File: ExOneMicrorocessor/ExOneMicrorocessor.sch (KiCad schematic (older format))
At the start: 33 parts, among them IC1 STM32G041C8T6, IC2 FT230XS, IC3 TLV73333PQDBVRQ1, J1 UJ2-MBH-3-SMT, J2 Conn_01x02, J3 02x03 Header, J4 01x03, J5 01x08, J6 01x10, J7 01x12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

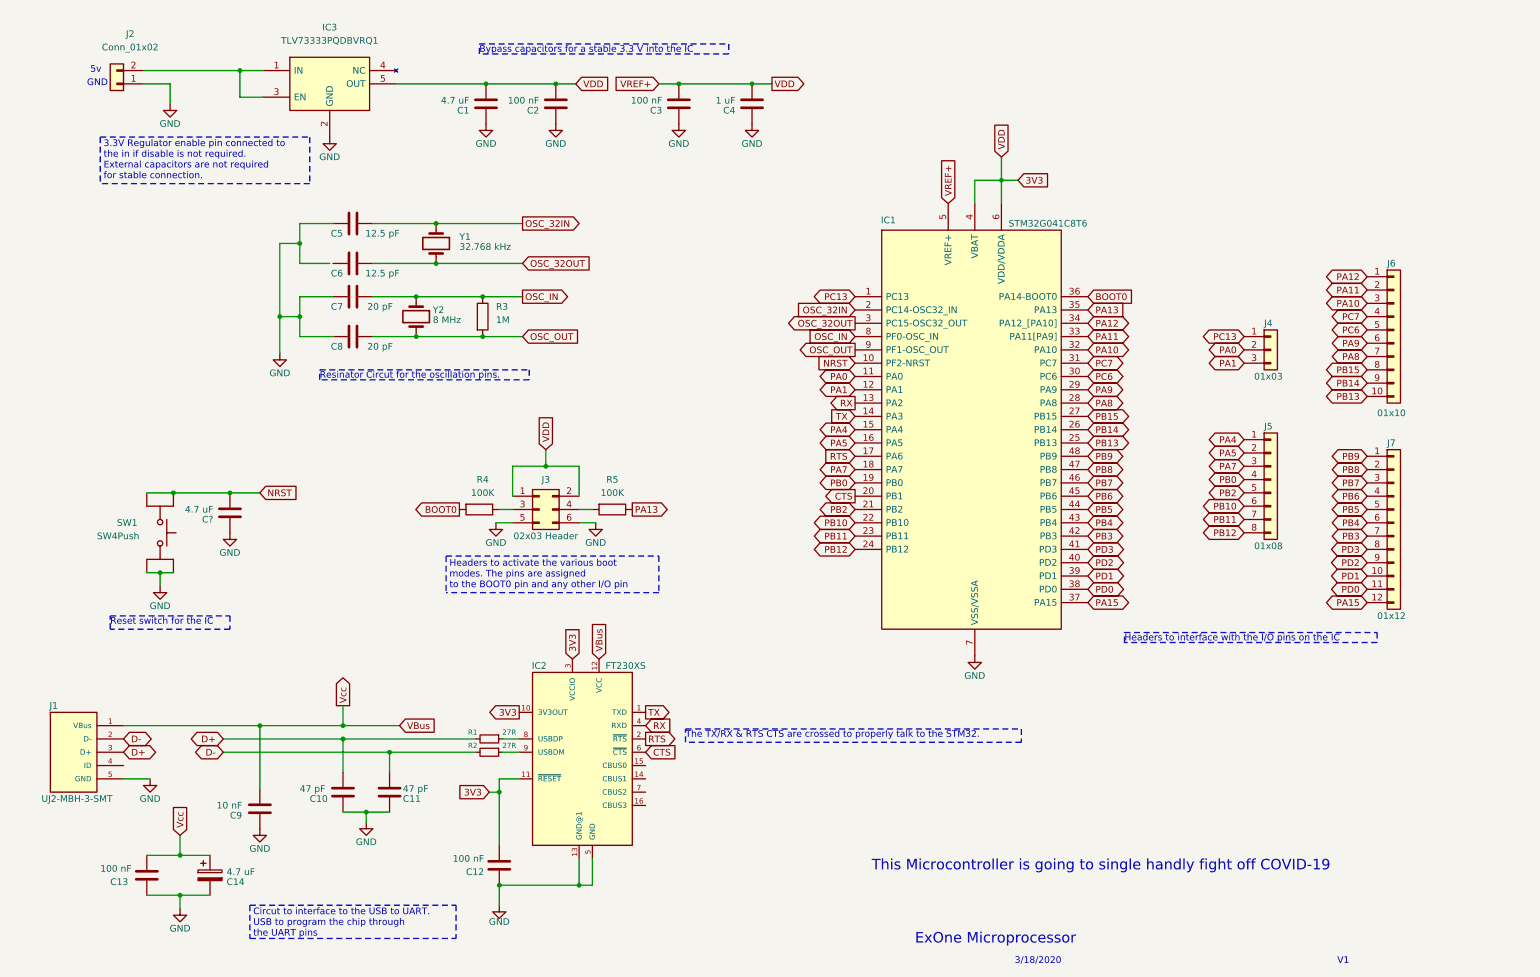
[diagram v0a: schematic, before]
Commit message: Updated Schematic
Updated net names

Added various notes explaning the design further

Changed the LDO IC
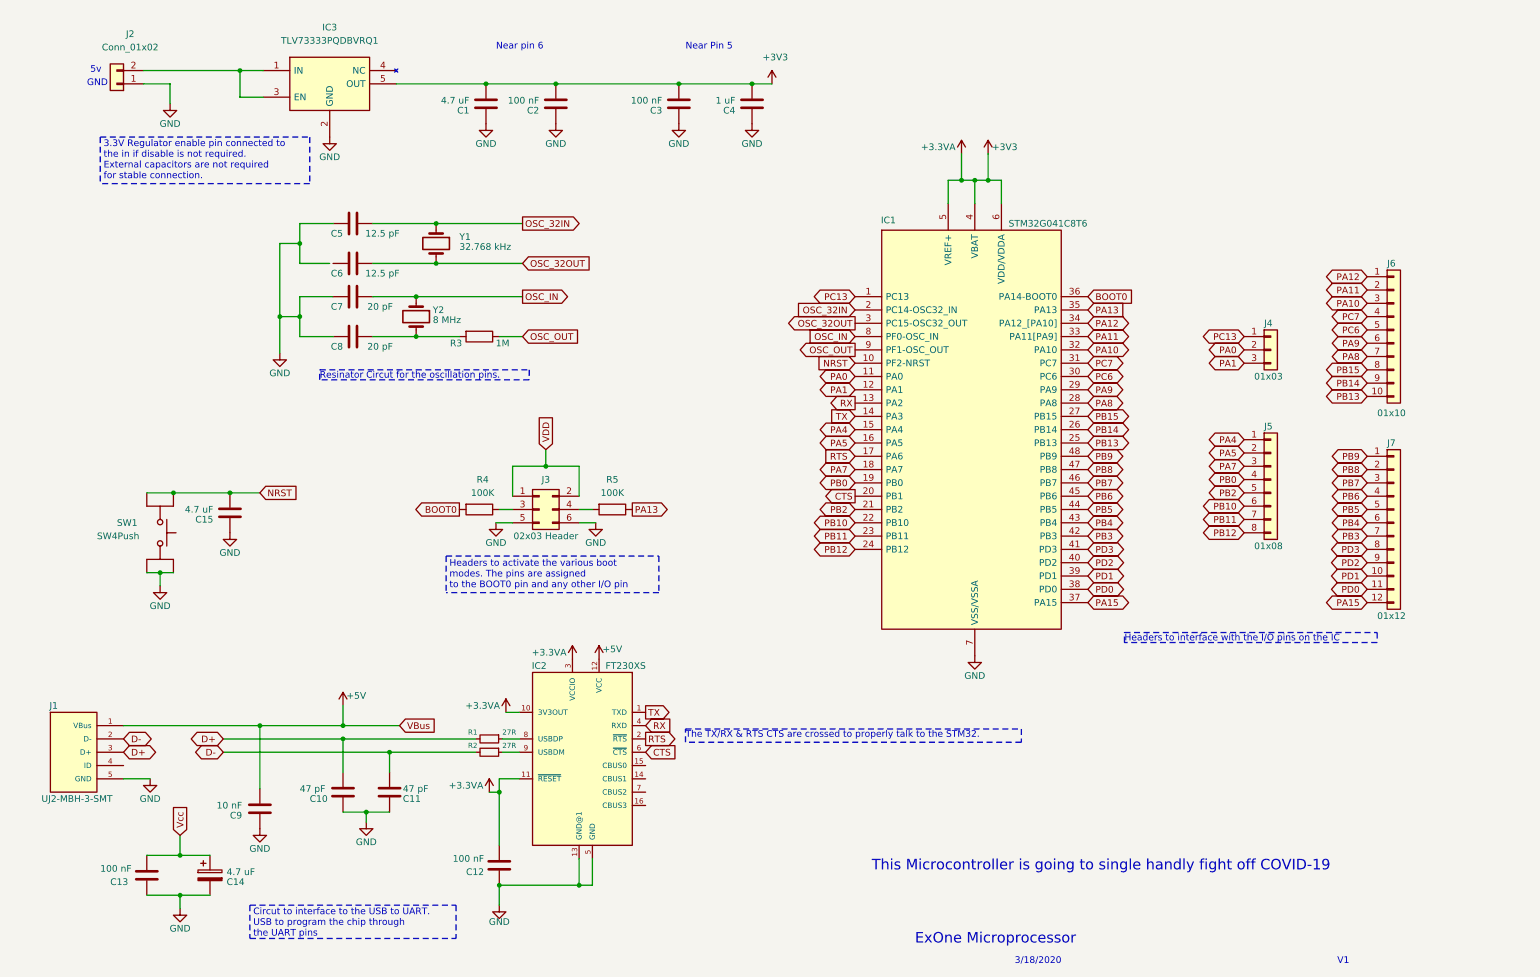
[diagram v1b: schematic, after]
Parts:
- gave numbers to parts that had none: 1
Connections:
- net OSC_IN: no longer R3.1
- net OSC_OUT: now also R3.1; no longer C8.2, R3.2, Y2.2
- net 3V3 renamed +3.3VA
- net +3.3VA: no longer J3.1 (Pin_1), J3.2 (Pin_2)
- net VBus renamed +5V
- net +5V: no longer C13.1, C14.1
- new net: C8.2, R3.2, Y2.2
- new net VDD: J3.1 (Pin_1), J3.2 (Pin_2)
- new net Vcc: C13.1, C14.1
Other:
- note added: "Near Pin 5"
- note added: "Near pin 6"
- note removed: "Bypass capacitors for a stable 3.3 V into the IC"
- note removed: "Reset switch for the IC"
- moved on the sheet: R3
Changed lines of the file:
@@
 	-1   0    0    1
 $EndComp
-Text GLabel 8050 1575 1    50   Input ~ 0
-VDD
-Text GLabel 4850 1025 2    50   Input ~ 0
-VDD
 $Comp
 L power:GND #PWR?
@@
 Wire Wire Line
 	4175 1025 4700 1025
-Wire Wire Line
-	4700 1025 4850 1025
 Connection ~ 4700 1025
 $Comp
@@
 	2325 925  2500 925
 Wire Wire Line
-	7850 1750 8050 1750
+	7850 1750 7950 1750
 Wire Wire Line
 	8050 1750 8050 1925
-Wire Wire Line
-	8050 1750 8050 1575
 $Comp
 L Device:C C4
@@
 Wire Wire Line
 	5625 1025 6175 1025
-Wire Wire Line
-	5475 1025 5625 1025
 Connection ~ 5625 1025
-Text GLabel 5475 1025 0    50   Input ~ 0
-VREF+
 $Comp
 L STM32G041C8T6:STM32G041C8T6 IC1
@@
 Wire Wire Line
 	7850 1750 7850 1925
-Text GLabel 7650 1925 1    50   Input ~ 0
-VREF+
 $Comp
 L power:GND #PWR?
@@
 	6325 1025 6175 1025
 Connection ~ 6175 1025
-Text GLabel 6325 1025 2    50   Output ~ 0
-VDD
 Text GLabel 3525 5850 2    50   Input ~ 0
 VBus
@@
 Text GLabel 6950 3025 0    50   Output ~ 0
 OSC_OUT
-Connection ~ 8050 1750
 Wire Wire Line
 	1600 925  2325 925
@@
 	1    0    0    -1
 $EndComp
-Text GLabel 4425 5750 0    50   Output ~ 0
-3V3
-Text GLabel 4825 5350 1    50   Input ~ 0
-3V3
 Wire Wire Line
 	4275 6250 4425 6250
@@
 Wire Wire Line
 	1450 5850 2475 5850
-Text GLabel 5025 5350 1    50   Input ~ 0
-VBus
 Wire Wire Line
 	2475 6325 2475 5850
@@
 Wire Wire Line
 	3100 5850 3525 5850
-Text GLabel 3100 5700 1    50   Output ~ 0
-Vcc
 Wire Wire Line
 	1875 6675 1875 6825
@@
 	2200 6050 3450 6050
 Connection ~ 3450 6050
-Text GLabel 8175 1750 2    50   Input ~ 0
-3V3
-Wire Wire Line
-	8050 1750 8175 1750
 Wire Wire Line
 	1625 4100 1825 4100
@@
 Connection ~ 1825 4100
 $Comp
-L Device:C C?
+L Device:C C15
 U 1 1 5E7F6799
 P 2250 4250
-F 0 "C?" H 2375 4300 50  0000 L CNN
+F 0 "C15" H 2375 4300 50  0000 L CNN
 F 1 "4.7 uF" H 2375 4225 50  0000 L CNN
 F 2 "" H 2288 4100 50  0001 C CNN
@@
 L Device:R R3
 U 1 1 5E82A971
-P 4150 2775
-F 0 "R3" H 4250 2850 50  0000 L CNN
-F 1 "1M" H 4250 2750 50  0000 L CNN
-F 2 "" V 4080 2775 50  0001 C CNN
-F 3 "~" H 4150 2775 50  0001 C CNN
-	1    4150 2775
-	1    0    0    -1
-$EndComp
-Connection ~ 3650 2625
-Connection ~ 3650 2925
-Wire Wire Line
-	3650 2925 4150 2925
-Wire Wire Line
-	3650 2625 4150 2625
-Connection ~ 4150 2625
-Connection ~ 4150 2925
-Wire Wire Line
-	4150 2625 4450 2625
-Wire Wire Line
-	4150 2925 4450 2925
+P 4125 2925
+F 0 "R3" V 4175 2750 50  0000 C CNN
+F 1 "1M" V 4175 3100 50  0000 C CNN
+F 2 "" V 4055 2925 50  0001 C CNN
+F 3 "~" H 4125 2925 50  0001 C CNN
+	1    4125 2925
+	0    1    1    0
+$EndComp
 $Comp
 L Connector_Generic:Conn_02x03_Odd_Even J3
@@
 Text GLabel 6950 3325 0    50   BiDi ~ 0
 PA1
-Text GLabel 4200 6350 0    50   Input ~ 0
-3V3
 Text GLabel 9875 3700 0    50   BiDi ~ 0
 PA4
@@
 Wire Notes Line
 	1275 1425 1275 1775
-Text Notes 4125 800  0    50   ~ 0
-Bypass capacitors for a stable 3.3 V into the IC
-Wire Notes Line
-	6000 800  4125 800
-Wire Notes Line
-	4125 800  4125 725
-Wire Notes Line
-	4125 725  6000 725
-Wire Notes Line
-	6000 725  6000 800
-Text Notes 1350 5100 0    50   ~ 0
-Reset switch for the IC
-Wire Notes Line
-	1350 5125 1350 5025
-Wire Notes Line
-	1350 5025 2250 5025
-Wire Notes Line
-	2250 5025 2250 5125
-Wire Notes Line
-	2250 5125 1350 5125
 Wire Notes Line
 	2400 7450 3950 7450
@@
 Text Notes 7400 7500 0    79   ~ 0
 ExOne Microprocessor
+Wire Wire Line
+	4700 1025 5625 1025
+$Comp
+L power:+3V3 #PWR?
+U 1 1 5E9FD0BE
+P 6325 1025
+F 0 "#PWR?" H 6325 875 50  0001 C CNN
+F 1 "+3V3" H 6350 1225 50  0000 C CNN
+F 2 "" H 6325 1025 50  0001 C CNN
+F 3 "" H 6325 1025 50  0001 C CNN
+	1    6325 1025
+	1    0    0    -1
+$EndComp
+Text Notes 5675 775  0    50   ~ 0
+Near Pin 5
+Text Notes 4250 775  0    50   ~ 0
+Near pin 6
+$Comp
+L power:+3V3 #PWR?
+U 1 1 5EA01841
+P 7950 1550
+F 0 "#PWR?" H 7950 1400 50  0001 C CNN
+F 1 "+3V3" H 8075 1600 50  0000 C CNN
+F 2 "" H 7950 1550 50  0001 C CNN
+F 3 "" H 7950 1550 50  0001 C CNN
+	1    7950 1550
+	1    0    0    -1
+$EndComp
+$Comp
+L power:+3.3VA #PWR?
+U 1 1 5EA06EA9
+P 7750 1550
+F 0 "#PWR?" H 7750 1400 50  0001 C CNN
+F 1 "+3.3VA" H 7575 1600 50  0000 C CNN
+F 2 "" H 7750 1550 50  0001 C CNN
+F 3 "" H 7750 1550 50  0001 C CNN
+	1    7750 1550
+	1    0    0    -1
+$EndComp
+Wire Wire Line
+	7650 1925 7650 1750
+Wire Wire Line
+	7650 1750 7750 1750
+Connection ~ 7850 1750
+Wire Wire Line
+	7950 1550 7950 1750
+Connection ~ 7950 1750
+Wire Wire Line
+	7950 1750 8050 1750
+Wire Wire Line
+	7750 1550 7750 1750
+Connection ~ 7750 1750
+Wire Wire Line
+	7750 1750 7850 1750
+$Comp
+L power:+3.3VA #PWR?
+U 1 1 5EA20DB3
+P 4200 6350
+F 0 "#PWR?" H 4200 6200 50  0001 C CNN
+F 1 "+3.3VA" H 4025 6400 50  0000 C CNN
+F 2 "" H 4200 6350 50  0001 C CNN
+F 3 "" H 4200 6350 50  0001 C CNN
+	1    4200 6350
+	1    0    0    -1
+$EndComp
+Wire Wire Line
+	4425 5750 4325 5750
+$Comp
+L power:+3.3VA #PWR?
+U 1 1 5EA24F20
+P 4325 5750
+F 0 "#PWR?" H 4325 5600 50  0001 C CNN
+F 1 "+3.3VA" H 4150 5800 50  0000 C CNN
+F 2 "" H 4325 5750 50  0001 C CNN
+F 3 "" H 4325 5750 50  0001 C CNN
+	1    4325 5750
+	1    0    0    -1
+$EndComp
+Wire Wire Line
+	4275 2925 4450 2925
+Connection ~ 3650 2625
+Wire Wire Line
+	3650 2625 4450 2625
+Wire Wire Line
+	3975 2925 3650 2925
+Connection ~ 3650 2925
+$Comp
+L power:+3.3VA #PWR?
+U 1 1 5EA582A4
+P 4825 5350
+F 0 "#PWR?" H 4825 5200 50  0001 C CNN
+F 1 "+3.3VA" H 4650 5400 50  0000 C CNN
+F 2 "" H 4825 5350 50  0001 C CNN
+F 3 "" H 4825 5350 50  0001 C CNN
+	1    4825 5350
+	1    0    0    -1
+$EndComp
+$Comp
+L power:+5V #PWR?
+U 1 1 5EA633B3
+P 3100 5700
+F 0 "#PWR?" H 3100 5550 50  0001 C CNN
+F 1 "+5V" H 3200 5775 50  0000 C CNN
+F 2 "" H 3100 5700 50  0001 C CNN
+F 3 "" H 3100 5700 50  0001 C CNN
+	1    3100 5700
+	1    0    0    -1
+$EndComp
+$Comp
+L power:+5V #PWR?
+U 1 1 5EA64F20
+P 5025 5350
+F 0 "#PWR?" H 5025 5200 50  0001 C CNN
+F 1 "+5V" H 5125 5425 50  0000 C CNN
+F 2 "" H 5025 5350 50  0001 C CNN
+F 3 "" H 5025 5350 50  0001 C CNN
+	1    5025 5350
+	1    0    0    -1
+$EndComp
 $EndSCHEMATC

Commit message: Just forgot to save it in the schema
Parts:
- removed IC3: TLV73333PQDBVRQ1, SOT95P280X145-5N, symbol TLV73333PQDBVRQ1:TLV73333PQDBVRQ1
- added C16: 0.1 uF, symbol Device:CP
- added C17: 10 uF, symbol Device:CP
- added R?: 250 k, symbol Device:R
- added U?: TPS77733DR, SOIC127P600X175-8N, symbol TPS77733DR:TPS77733DR
- R4, R5: value 100K -> 100R
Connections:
- net +3.3VA: now also J2.2 (Pin_2), C16.1, U?.3 (IN_2), U?.4 (IN); no longer C1.2, C2.2, C3.2, C4.2, IC1.4 (VBAT), IC1.5 (VREF+), IC1.6 (VDD/VDDA)
- net GND: now also C16.2, C17.2, U?.1 (GND), U?.2 (~EN)
- new net: R?.2, U?.8 (~RESET/PG)
- new net +3V3: C1.2, C17.1, C2.2, C3.2, C4.2, IC1.4 (VBAT), IC1.5 (VREF+), IC1.6 (VDD/VDDA), R?.1, U?.5 (OUT_2), U?.6 (OUT)
- no-connect marks 0 -> 1
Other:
- note added: "*Note: The resistor value is dependant\non the properties of the crystal and \nexact crystal is unkown as of now"
- note added: "+"
- note added: "-"
- note added: "3.3V Regulator enable pin connected to\nground if not needed. \n"
- note added: "Board can be powered via USB or\nthrough a connector. The LDO is rated\nfor up to 10 volts and Outputs 3.3V at\n750 mA. Power from UART Chip and \nexternal power is routed here to regulate\nit to 3.3 volts."
- note added: "ExOne Board"
- note added: "The IC has an internal pull up resistor. \nAn external resistor is not required for \nthe switch"
- note added: "This Board is going to single handly fight off COVID-19"
- note removed: "3.3V Regulator enable pin connected to \nthe in if disable is not required.\nExternal capacitors are not required\nfor stable connection."
- note removed: "5v"
- note removed: "ExOne Microprocessor"
- note removed: "GND"
- note removed: "This Microcontroller is going to single handly fight off COVID-19"
- moved on the sheet: C1, C2, C3, C4, C5, C6, C7, C8, J2, R3, Y1, Y2
